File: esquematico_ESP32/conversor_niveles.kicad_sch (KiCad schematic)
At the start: 6 parts, among them Q1 BSS138, Q2 BSS138

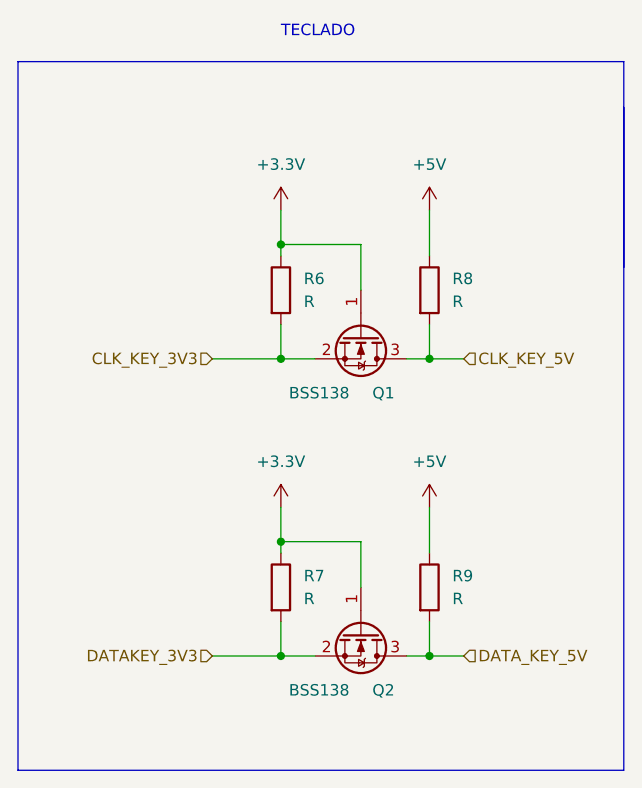
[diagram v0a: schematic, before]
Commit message: se agregaron los valores (pendiente última revisión)
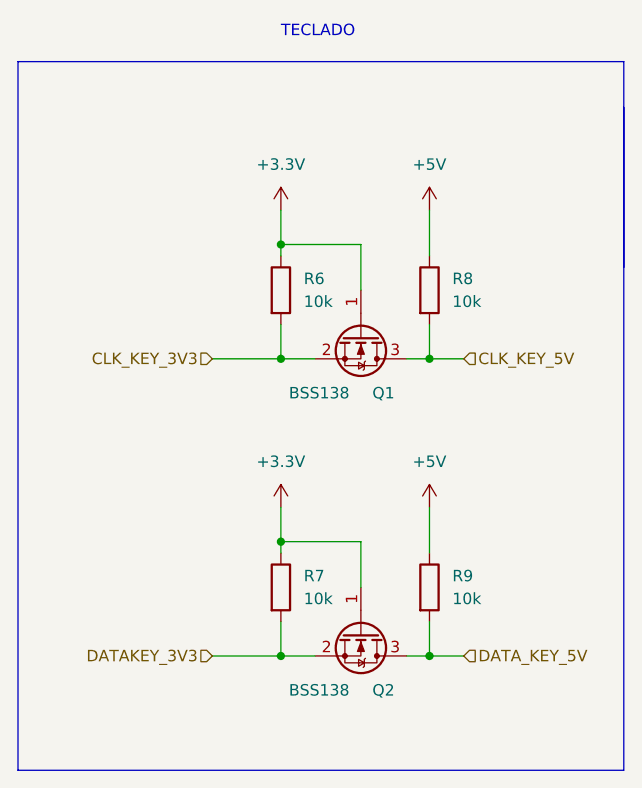
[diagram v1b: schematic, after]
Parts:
- R6, R7, R8, R9: value R -> 10k
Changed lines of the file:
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@@
       (effects (font (size 1.27 1.27)) (justify left))
     )
-    (property "Value" "R" (id 1) (at 146.05 77.4699 0)
+    (property "Value" "10k" (id 1) (at 146.05 77.4699 0)
       (effects (font (size 1.27 1.27)) (justify left))
     )
@@
       (effects (font (size 1.27 1.27)) (justify left))
     )
-    (property "Value" "R" (id 1) (at 146.05 110.4899 0)
+    (property "Value" "10k" (id 1) (at 146.05 110.4899 0)
       (effects (font (size 1.27 1.27)) (justify left))
     )
@@
       (effects (font (size 1.27 1.27)) (justify left))
     )
-    (property "Value" "R" (id 1) (at 162.56 110.4899 0)
+    (property "Value" "10k" (id 1) (at 162.56 110.4899 0)
       (effects (font (size 1.27 1.27)) (justify left))
     )
@@
       (effects (font (size 1.27 1.27)) (justify left))
     )
-    (property "Value" "R" (id 1) (at 162.56 77.4699 0)
+    (property "Value" "10k" (id 1) (at 162.56 77.4699 0)
       (effects (font (size 1.27 1.27)) (justify left))
     )
